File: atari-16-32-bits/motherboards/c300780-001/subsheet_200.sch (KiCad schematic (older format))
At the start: 23 parts, among them J200 DIN5 — MIDI OUT/THRU, J201 DIN5 — MIDI IN, U200 MC6850_PHY, U208 PC900_PHY, U210 7406_PHY

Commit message: [PCB] Assign builtins footprint when possible - resistors, ports
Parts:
- D202: footprint (none) -> Diode_THT:D_DO-35_SOD27_P7.62mm_Horizontal
- R200, R201, R202, R204, R205, R207, R218, R219: footprint (none) -> Resistor_THT:R_Axial_DIN0204_L3.6mm_D1.6mm_P7.62mm_Horizontal
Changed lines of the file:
@@
 F 0 "D202" V 4750 6200 50  0000 C CNN
 F 1 "1N914" V 4850 6200 50  0000 C CNN
-F 2 "" H 4800 6400 50  0001 C CNN
+F 2 "Diode_THT:D_DO-35_SOD27_P7.62mm_Horizontal" H 4800 6400 50  0001 C CNN
 F 3 "~" H 4800 6400 50  0001 C CNN
 	1    4800 6400
@@
 F 0 "R200" V 2650 4250 50  0000 C CNN
 F 1 "220" V 2750 4250 50  0000 C CNN
-F 2 "" H 2700 4400 50  0001 C CNN
+F 2 "Resistor_THT:R_Axial_DIN0204_L3.6mm_D1.6mm_P7.62mm_Horizontal" H 2700 4400 50  0001 C CNN
 F 3 "~" H 2700 4400 50  0001 C CNN
 	1    2700 4400
@@
 F 0 "R205" V 2650 4500 50  0000 C CNN
 F 1 "220" V 2750 4500 50  0000 C CNN
-F 2 "" H 2700 4650 50  0001 C CNN
+F 2 "Resistor_THT:R_Axial_DIN0204_L3.6mm_D1.6mm_P7.62mm_Horizontal" H 2700 4650 50  0001 C CNN
 F 3 "~" H 2700 4650 50  0001 C CNN
 	1    2700 4650
@@
 F 0 "R202" V 2650 4750 50  0000 C CNN
 F 1 "220" V 2750 4750 50  0000 C CNN
-F 2 "" H 2700 4900 50  0001 C CNN
+F 2 "Resistor_THT:R_Axial_DIN0204_L3.6mm_D1.6mm_P7.62mm_Horizontal" H 2700 4900 50  0001 C CNN
 F 3 "~" H 2700 4900 50  0001 C CNN
 	1    2700 4900
@@
 F 0 "R204" V 2650 5000 50  0000 C CNN
 F 1 "220" V 2750 5000 50  0000 C CNN
-F 2 "" H 2700 5150 50  0001 C CNN
+F 2 "Resistor_THT:R_Axial_DIN0204_L3.6mm_D1.6mm_P7.62mm_Horizontal" H 2700 5150 50  0001 C CNN
 F 3 "~" H 2700 5150 50  0001 C CNN
 	1    2700 5150
@@
 F 0 "R218" H 5850 3200 50  0000 C CNN
 F 1 "4K7" H 5850 3300 50  0000 C CNN
-F 2 "" H 6000 3250 50  0001 C CNN
+F 2 "Resistor_THT:R_Axial_DIN0204_L3.6mm_D1.6mm_P7.62mm_Horizontal" H 6000 3250 50  0001 C CNN
 F 3 "~" H 6000 3250 50  0001 C CNN
 	1    6000 3250
@@
 F 0 "R219" H 6350 3200 50  0000 C CNN
 F 1 "4K7" H 6350 3300 50  0000 C CNN
-F 2 "" H 6500 3250 50  0001 C CNN
+F 2 "Resistor_THT:R_Axial_DIN0204_L3.6mm_D1.6mm_P7.62mm_Horizontal" H 6500 3250 50  0001 C CNN
 F 3 "~" H 6500 3250 50  0001 C CNN
 	1    6500 3250
@@
 F 0 "R207" V 4200 6150 50  0000 C CNN
 F 1 "220" V 4400 6150 50  0000 C CNN
-F 2 "" H 4300 6150 50  0001 C CNN
+F 2 "Resistor_THT:R_Axial_DIN0204_L3.6mm_D1.6mm_P7.62mm_Horizontal" H 4300 6150 50  0001 C CNN
 F 3 "~" H 4300 6150 50  0001 C CNN
 	1    4300 6150
@@
 F 0 "R201" H 5350 3200 50  0000 C CNN
 F 1 "4K7" H 5350 3300 50  0000 C CNN
-F 2 "" H 5500 3250 50  0001 C CNN
+F 2 "Resistor_THT:R_Axial_DIN0204_L3.6mm_D1.6mm_P7.62mm_Horizontal" H 5500 3250 50  0001 C CNN
 F 3 "~" H 5500 3250 50  0001 C CNN
 	1    5500 3250

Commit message: Resolves #41 : [PCB] custom footprint library for passives
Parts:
- D202: footprint Diode_THT:D_DO-35_SOD27_P7.62mm_Horizontal -> commons_passives_THT:Passive_THT_diode_W2.54mm_L12.70mm
- L200, L201, L202, L204, L205, L206: footprint (none) -> commons_passives_THT:Passive_THT_EMI_filter_W5.08mm_L7.62mm
- R200, R201, R202, R204, R205, R207, R218, R219: footprint Resistor_THT:R_Axial_DIN0204_L3.6mm_D1.6mm_P7.62mm_Horizontal -> commons_passives_THT:Passive_THT_resistor_W2.54mm_L12.70mm
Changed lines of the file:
@@
 F 0 "D202" V 4750 6200 50  0000 C CNN
 F 1 "1N914" V 4850 6200 50  0000 C CNN
-F 2 "Diode_THT:D_DO-35_SOD27_P7.62mm_Horizontal" H 4800 6400 50  0001 C CNN
+F 2 "commons_passives_THT:Passive_THT_diode_W2.54mm_L12.70mm" H 4800 6400 50  0001 C CNN
 F 3 "~" H 4800 6400 50  0001 C CNN
 	1    4800 6400
@@
 F 0 "R200" V 2650 4250 50  0000 C CNN
 F 1 "220" V 2750 4250 50  0000 C CNN
-F 2 "Resistor_THT:R_Axial_DIN0204_L3.6mm_D1.6mm_P7.62mm_Horizontal" H 2700 4400 50  0001 C CNN
+F 2 "commons_passives_THT:Passive_THT_resistor_W2.54mm_L12.70mm" H 2700 4400 50  0001 C CNN
 F 3 "~" H 2700 4400 50  0001 C CNN
 	1    2700 4400
@@
 F 0 "R205" V 2650 4500 50  0000 C CNN
 F 1 "220" V 2750 4500 50  0000 C CNN
-F 2 "Resistor_THT:R_Axial_DIN0204_L3.6mm_D1.6mm_P7.62mm_Horizontal" H 2700 4650 50  0001 C CNN
+F 2 "commons_passives_THT:Passive_THT_resistor_W2.54mm_L12.70mm" H 2700 4650 50  0001 C CNN
 F 3 "~" H 2700 4650 50  0001 C CNN
 	1    2700 4650
@@
 F 0 "R202" V 2650 4750 50  0000 C CNN
 F 1 "220" V 2750 4750 50  0000 C CNN
-F 2 "Resistor_THT:R_Axial_DIN0204_L3.6mm_D1.6mm_P7.62mm_Horizontal" H 2700 4900 50  0001 C CNN
+F 2 "commons_passives_THT:Passive_THT_resistor_W2.54mm_L12.70mm" H 2700 4900 50  0001 C CNN
 F 3 "~" H 2700 4900 50  0001 C CNN
 	1    2700 4900
@@
 F 0 "R204" V 2650 5000 50  0000 C CNN
 F 1 "220" V 2750 5000 50  0000 C CNN
-F 2 "Resistor_THT:R_Axial_DIN0204_L3.6mm_D1.6mm_P7.62mm_Horizontal" H 2700 5150 50  0001 C CNN
+F 2 "commons_passives_THT:Passive_THT_resistor_W2.54mm_L12.70mm" H 2700 5150 50  0001 C CNN
 F 3 "~" H 2700 5150 50  0001 C CNN
 	1    2700 5150
@@
 F 0 "R218" H 5850 3200 50  0000 C CNN
 F 1 "4K7" H 5850 3300 50  0000 C CNN
-F 2 "Resistor_THT:R_Axial_DIN0204_L3.6mm_D1.6mm_P7.62mm_Horizontal" H 6000 3250 50  0001 C CNN
+F 2 "commons_passives_THT:Passive_THT_resistor_W2.54mm_L12.70mm" H 6000 3250 50  0001 C CNN
 F 3 "~" H 6000 3250 50  0001 C CNN
 	1    6000 3250
@@
 F 0 "R219" H 6350 3200 50  0000 C CNN
 F 1 "4K7" H 6350 3300 50  0000 C CNN
-F 2 "Resistor_THT:R_Axial_DIN0204_L3.6mm_D1.6mm_P7.62mm_Horizontal" H 6500 3250 50  0001 C CNN
+F 2 "commons_passives_THT:Passive_THT_resistor_W2.54mm_L12.70mm" H 6500 3250 50  0001 C CNN
 F 3 "~" H 6500 3250 50  0001 C CNN
 	1    6500 3250
@@
 F 0 "L200" H 3300 4775 50  0000 C CNN
 F 1 "EMI_Filter_LCL" H 3300 4700 50  0000 C CNN
-F 2 "" V 3300 4500 50  0001 C CNN
+F 2 "commons_passives_THT:Passive_THT_EMI_filter_W5.08mm_L7.62mm" V 3300 4500 50  0001 C CNN
 F 3 "http://www.murata.com/~/media/webrenewal/support/library/catalog/products/emc/emifil/c31e.ashx?la=en-gb" V 3300 4500 50  0001 C CNN
 	1    3300 4500
@@
 F 0 "L201" H 4050 5025 50  0000 C CNN
 F 1 "EMI_Filter_LCL" H 4050 4950 50  0000 C CNN
-F 2 "" V 4050 4750 50  0001 C CNN
+F 2 "commons_passives_THT:Passive_THT_EMI_filter_W5.08mm_L7.62mm" V 4050 4750 50  0001 C CNN
 F 3 "http://www.murata.com/~/media/webrenewal/support/library/catalog/products/emc/emifil/c31e.ashx?la=en-gb" V 4050 4750 50  0001 C CNN
 	1    4050 4750
@@
 F 0 "L202" H 3300 5275 50  0000 C CNN
 F 1 "EMI_Filter_LCL" H 3300 5200 50  0000 C CNN
-F 2 "" V 3300 5000 50  0001 C CNN
+F 2 "commons_passives_THT:Passive_THT_EMI_filter_W5.08mm_L7.62mm" V 3300 5000 50  0001 C CNN
 F 3 "http://www.murata.com/~/media/webrenewal/support/library/catalog/products/emc/emifil/c31e.ashx?la=en-gb" V 3300 5000 50  0001 C CNN
 	1    3300 5000
@@
 F 0 "L204" H 4050 5525 50  0000 C CNN
 F 1 "EMI_Filter_LCL" H 4050 5450 50  0000 C CNN
-F 2 "" V 4050 5250 50  0001 C CNN
+F 2 "commons_passives_THT:Passive_THT_EMI_filter_W5.08mm_L7.62mm" V 4050 5250 50  0001 C CNN
 F 3 "http://www.murata.com/~/media/webrenewal/support/library/catalog/products/emc/emifil/c31e.ashx?la=en-gb" V 4050 5250 50  0001 C CNN
 	1    4050 5250
@@
 F 0 "R207" V 4200 6150 50  0000 C CNN
 F 1 "220" V 4400 6150 50  0000 C CNN
-F 2 "Resistor_THT:R_Axial_DIN0204_L3.6mm_D1.6mm_P7.62mm_Horizontal" H 4300 6150 50  0001 C CNN
+F 2 "commons_passives_THT:Passive_THT_resistor_W2.54mm_L12.70mm" H 4300 6150 50  0001 C CNN
 F 3 "~" H 4300 6150 50  0001 C CNN
 	1    4300 6150
@@
 F 0 "L205" H 5300 6525 50  0000 C CNN
 F 1 "EMI_Filter_LCL" H 5300 6450 50  0000 C CNN
-F 2 "" V 5300 6250 50  0001 C CNN
+F 2 "commons_passives_THT:Passive_THT_EMI_filter_W5.08mm_L7.62mm" V 5300 6250 50  0001 C CNN
 F 3 "http://www.murata.com/~/media/webrenewal/support/library/catalog/products/emc/emifil/c31e.ashx?la=en-gb" V 5300 6250 50  0001 C CNN
 	1    5300 6250
@@
 F 0 "L206" H 5300 7025 50  0000 C CNN
 F 1 "EMI_Filter_LCL" H 5300 6950 50  0000 C CNN
-F 2 "" V 5300 6750 50  0001 C CNN
+F 2 "commons_passives_THT:Passive_THT_EMI_filter_W5.08mm_L7.62mm" V 5300 6750 50  0001 C CNN
 F 3 "http://www.murata.com/~/media/webrenewal/support/library/catalog/products/emc/emifil/c31e.ashx?la=en-gb" V 5300 6750 50  0001 C CNN
 	1    5300 6750
@@
 F 0 "R201" H 5350 3200 50  0000 C CNN
 F 1 "4K7" H 5350 3300 50  0000 C CNN
-F 2 "Resistor_THT:R_Axial_DIN0204_L3.6mm_D1.6mm_P7.62mm_Horizontal" H 5500 3250 50  0001 C CNN
+F 2 "commons_passives_THT:Passive_THT_resistor_W2.54mm_L12.70mm" H 5500 3250 50  0001 C CNN
 F 3 "~" H 5500 3250 50  0001 C CNN
 	1    5500 3250

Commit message: [PCB] continue footprint assignation
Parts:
- C200, C201, C227: footprint (none) -> commons_passives_THT:Passive_THT_capacitor_ceramic_radial_W5.08mm_L6.35mm_X11.43mm
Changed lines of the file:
@@
 F 0 "C200" H 7025 3350 50  0000 L CNN
 F 1 "0.1uF" H 7025 3150 50  0000 L CNN
-F 2 "" H 7038 3100 50  0001 C CNN
+F 2 "commons_passives_THT:Passive_THT_capacitor_ceramic_radial_W5.08mm_L6.35mm_X11.43mm" H 7038 3100 50  0001 C CNN
 F 3 "~" H 7000 3250 50  0001 C CNN
 	1    7000 3250
@@
 F 0 "C201" H 1275 3350 50  0000 L CNN
 F 1 "0.1uF" H 1275 3150 50  0000 L CNN
-F 2 "" H 1288 3100 50  0001 C CNN
+F 2 "commons_passives_THT:Passive_THT_capacitor_ceramic_radial_W5.08mm_L6.35mm_X11.43mm" H 1288 3100 50  0001 C CNN
 F 3 "~" H 1250 3250 50  0001 C CNN
 	1    1250 3250
@@
 F 0 "C227" H 7125 2250 50  0000 L CNN
 F 1 "0.1uF" H 7125 2050 50  0000 L CNN
-F 2 "" H 7138 2000 50  0001 C CNN
+F 2 "commons_passives_THT:Passive_THT_capacitor_ceramic_radial_W5.08mm_L6.35mm_X11.43mm" H 7138 2000 50  0001 C CNN
 F 3 "~" H 7100 2150 50  0001 C CNN
 	1    7100 2150

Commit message: [PCB] continue assigning footprints + special libraries of special holes referenced in the measurement schema of the field service manual
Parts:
- J200, J201: footprint (none) -> commons-interconnect_THT:socket-din-5
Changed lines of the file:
@@
 F 0 "J200" H 6250 5050 50  0000 C CNN
 F 1 "DIN5 — MIDI OUT/THRU" H 6250 4450 50  0000 C CNN
-F 2 "" H 6250 4750 50  0001 C CNN
+F 2 "commons-interconnect_THT:socket-din-5" H 6250 4750 50  0001 C CNN
 F 3 "~" H 6250 4750 50  0001 C CNN
 	1    6250 4750
@@
 F 0 "J201" H 6250 6350 50  0000 C CNN
 F 1 "DIN5 — MIDI IN" H 6250 5750 50  0000 C CNN
-F 2 "" H 6250 6050 50  0001 C CNN
+F 2 "commons-interconnect_THT:socket-din-5" H 6250 6050 50  0001 C CNN
 F 3 "~" H 6250 6050 50  0001 C CNN
 	1    6250 6050

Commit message: Resolves #45 : [Atari STE]Use shielded connectors
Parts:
- J200: value DIN5 — MIDI OUT/THRU -> DIN-5S — MIDI OUT/THRU; symbol Connector_Generic:Conn_01x05 -> Connector_Generic_Shielded:Conn_01x05_Shielded
- J201: value DIN5 — MIDI IN -> DIN-5S — MIDI IN; symbol Connector_Generic:Conn_01x05 -> Connector_Generic_Shielded:Conn_01x05_Shielded
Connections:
- wire segments 88 -> 90
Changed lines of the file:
@@
 	2800 5150 3750 5150
 $Comp
-L Connector_Generic:Conn_01x05 J200
+L Connector_Generic_Shielded:Conn_01x05_Shielded J200
 U 1 1 611055AA
 P 6250 4750
 F 0 "J200" H 6250 5050 50  0000 C CNN
-F 1 "DIN5 — MIDI OUT/THRU" H 6250 4450 50  0000 C CNN
+F 1 "DIN-5S — MIDI OUT/THRU" H 6250 5150 50  0000 C CNN
 F 2 "commons-interconnect_THT:socket-din-5" H 6250 4750 50  0001 C CNN
 F 3 "~" H 6250 4750 50  0001 C CNN
@@
 	4050 6250 4050 6650
 $Comp
-L Connector_Generic:Conn_01x05 J201
+L Connector_Generic_Shielded:Conn_01x05_Shielded J201
 U 1 1 61143C4D
 P 6250 6050
 F 0 "J201" H 6250 6350 50  0000 C CNN
-F 1 "DIN5 — MIDI IN" H 6250 5750 50  0000 C CNN
+F 1 "DIN-5S — MIDI IN" H 6250 6450 50  0000 C CNN
 F 2 "commons-interconnect_THT:socket-din-5" H 6250 6050 50  0001 C CNN
 F 3 "~" H 6250 6050 50  0001 C CNN
@@
 Wire Wire Line
 	6500 2900 6500 3150
+Text Label 6250 5350 1    50   ~ 0
+GND
+Wire Wire Line
+	6250 5350 6250 5150
+Text Label 6250 6650 1    50   ~ 0
+GND
+Wire Wire Line
+	6250 6650 6250 6450
 $EndSCHEMATC

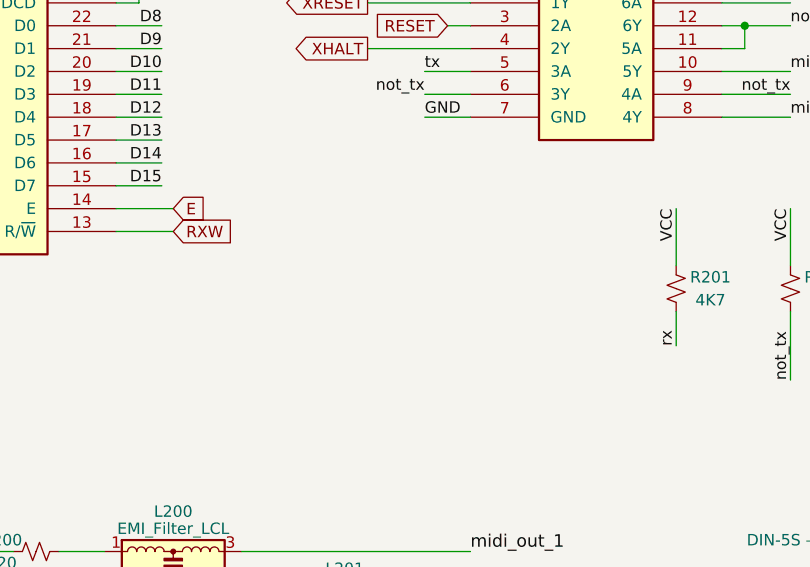
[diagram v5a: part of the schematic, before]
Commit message: Fixed : missing R209, pull up U200 and U201 IRQ
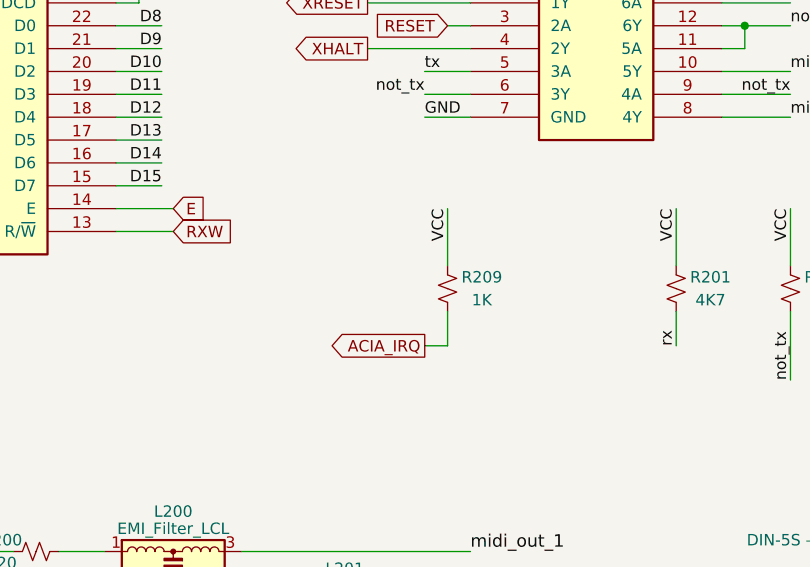
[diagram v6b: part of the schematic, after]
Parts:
- added R209: 1K, commons_passives_THT:Passive_THT_resistor_W2.54mm_L12.70mm, symbol Device:R_Small_US
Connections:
- net ACIA_IRQ: now also R209.1
- net VCC: now also R209.2
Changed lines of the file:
@@
 Wire Wire Line
 	6250 6650 6250 6450
+Text Label 4500 2900 3    50   ~ 0
+VCC
+$Comp
+L Device:R_Small_US R209
+U 1 1 60EF9181
+P 4500 3250
+F 0 "R209" H 4350 3200 50  0000 C CNN
+F 1 "1K" H 4350 3300 50  0000 C CNN
+F 2 "commons_passives_THT:Passive_THT_resistor_W2.54mm_L12.70mm" H 4500 3250 50  0001 C CNN
+F 3 "~" H 4500 3250 50  0001 C CNN
+	1    4500 3250
+	-1   0    0    1
+$EndComp
+Wire Wire Line
+	4500 2900 4500 3150
+Text GLabel 4400 3500 0    50   Output ~ 0
+ACIA_IRQ
+Wire Wire Line
+	4500 3350 4500 3500
+Wire Wire Line
+	4400 3500 4500 3500
 $EndSCHEMATC
